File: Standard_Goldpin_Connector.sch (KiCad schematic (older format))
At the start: 1 part, among them P1 Display Connector

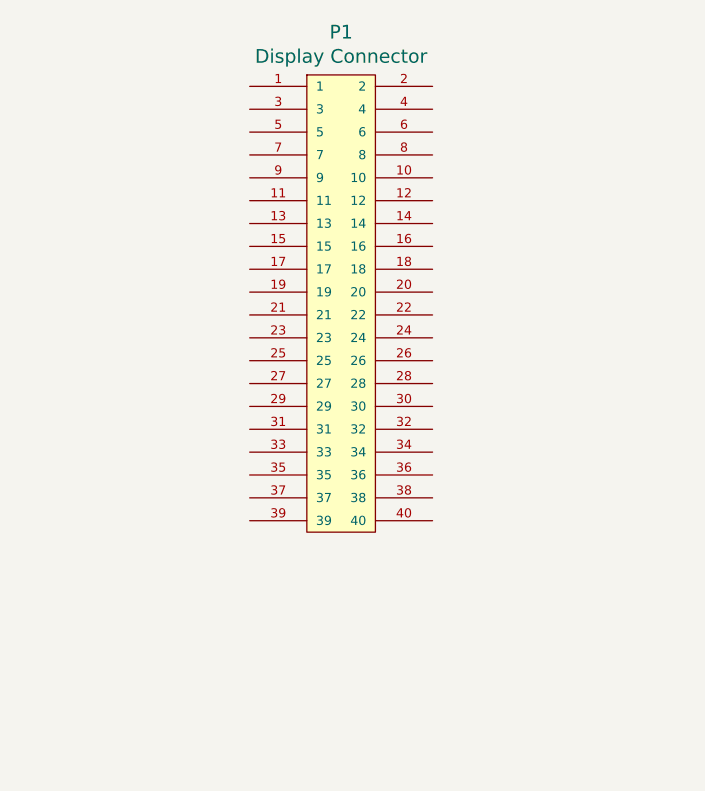
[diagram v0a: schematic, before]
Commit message: Filled hierarchical sheets
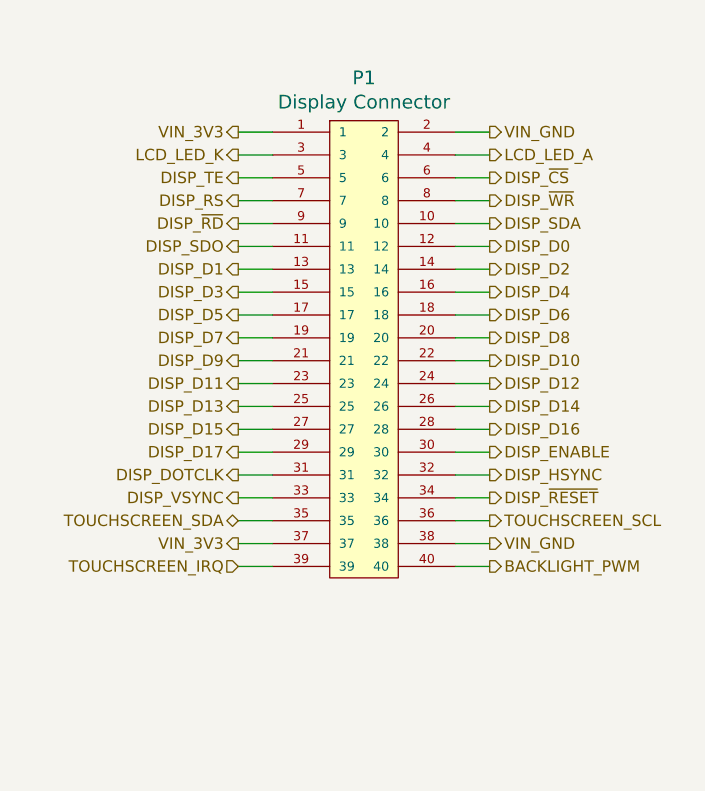
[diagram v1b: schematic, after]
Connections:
- net VIN_3V3: now reaches P1.1
- net VIN_3V3: now also P1.37
- net DISP_SDA: now reaches P1.10
- net DISP_SDO: now reaches P1.11
- net DISP_D0: now reaches P1.12
- net DISP_D1: now reaches P1.13
- net DISP_D2: now reaches P1.14
- net DISP_D3: now reaches P1.15
- net DISP_D4: now reaches P1.16
- net DISP_D5: now reaches P1.17
- net DISP_D6: now reaches P1.18
- net DISP_D7: now reaches P1.19
- net VIN_GND: now reaches P1.2
- net VIN_GND: now also P1.38
- net DISP_D8: now reaches P1.20
- net DISP_D9: now reaches P1.21
- net DISP_D10: now reaches P1.22
- net DISP_D11: now reaches P1.23
- net DISP_D12: now reaches P1.24
- net DISP_D13: now reaches P1.25
- net DISP_D14: now reaches P1.26
- net DISP_D15: now reaches P1.27
- net DISP_D16: now reaches P1.28
- net DISP_D17: now reaches P1.29
- net LCD_LED_K: now reaches P1.3
- net DISP_ENABLE: now reaches P1.30
- net DISP_DOTCLK: now reaches P1.31
- net DISP_HSYNC: now reaches P1.32
- net DISP_VSYNC: now reaches P1.33
- net DISP_~RESET~: now reaches P1.34
- net TOUCHSCREEN_SDA: now reaches P1.35
- net TOUCHSCREEN_SCL: now reaches P1.36
- net TOUCHSCREEN_IRQ: now reaches P1.39
- net LCD_LED_A: now reaches P1.4
- net BACKLIGHT_PWM: now reaches P1.40
- net DISP_TE: now reaches P1.5
- net DISP_~CS~: now reaches P1.6
- net DISP_RS: now reaches P1.7
- net DISP_~WR~: now reaches P1.8
- net DISP_~RD~: now reaches P1.9
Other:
- moved on the sheet: P1
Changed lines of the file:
@@
 $Descr A3 16535 11693
 encoding utf-8
-Sheet 5 5
+Sheet 4 5
 Title "Goldpin Display Connector"
 Date "2020-07-08"
@@
 L Goldpin_2_54mm:GOLDPIN_20_2_2_54MM P1
 U 1 1 5F087B95
-P 8200 5500
-F 0 "P1" H 8200 6687 60  0000 C CNN
-F 1 "Display Connector" H 8200 6581 60  0000 C CNN
-F 2 "Goldpin:Goldpin_20_2_2_54mm_SMT" H 9500 6100 60  0001 C CNN
-F 3 "Goldpins/Components_Documentation/Goldpin_2_54mm.pdf" H 8200 6581 60  0001 C CNN
-	1    8200 5500
+P 8300 5700
+F 0 "P1" H 8300 6887 60  0000 C CNN
+F 1 "Display Connector" H 8300 6781 60  0000 C CNN
+F 2 "Goldpin:Goldpin_20_2_2_54mm_SMT" H 9600 6300 60  0001 C CNN
+F 3 "Goldpins/Components_Documentation/Goldpin_2_54mm.pdf" H 8300 6781 60  0001 C CNN
+	1    8300 5700
 	1    0    0    -1
 $EndComp
+Text HLabel 7750 6650 0    50   Input ~ 0
+TOUCHSCREEN_IRQ
+Text HLabel 7750 6450 0    50   BiDi ~ 0
+TOUCHSCREEN_SDA
+Text HLabel 8850 6450 2    50   Output ~ 0
+TOUCHSCREEN_SCL
+Text HLabel 7750 4750 0    50   Output ~ 0
+VIN_3V3
+Text HLabel 8850 4750 2    50   Output ~ 0
+VIN_GND
+Text HLabel 8850 6650 2    50   Output ~ 0
+BACKLIGHT_PWM
+Text HLabel 7750 4950 0    50   Output ~ 0
+DISP_TE
+Text HLabel 8850 4950 2    50   Output ~ 0
+DISP_~CS~
+Text HLabel 7750 5050 0    50   Output ~ 0
+DISP_RS
+Text HLabel 8850 5050 2    50   Output ~ 0
+DISP_~WR~
+Text HLabel 7750 5150 0    50   Output ~ 0
+DISP_~RD~
+Text HLabel 8850 5150 2    50   Output ~ 0
+DISP_SDA
+Text HLabel 7750 5250 0    50   Output ~ 0
+DISP_SDO
+Text HLabel 8850 5250 2    50   Output ~ 0
+DISP_D0
+Text HLabel 7750 5350 0    50   Output ~ 0
+DISP_D1
+Text HLabel 8850 5350 2    50   Output ~ 0
+DISP_D2
+Text HLabel 7750 5450 0    50   Output ~ 0
+DISP_D3
+Text HLabel 8850 5450 2    50   Output ~ 0
+DISP_D4
+Text HLabel 7750 5550 0    50   Output ~ 0
+DISP_D5
+Text HLabel 8850 5550 2    50   Output ~ 0
+DISP_D6
+Text HLabel 7750 5650 0    50   Output ~ 0
+DISP_D7
+Text HLabel 8850 5650 2    50   Output ~ 0
+DISP_D8
+Text HLabel 7750 5750 0    50   Output ~ 0
+DISP_D9
+Text HLabel 8850 5750 2    50   Output ~ 0
+DISP_D10
+Text HLabel 7750 5850 0    50   Output ~ 0
+DISP_D11
+Text HLabel 8850 5850 2    50   Output ~ 0
+DISP_D12
+Text HLabel 7750 5950 0    50   Output ~ 0
+DISP_D13
+Text HLabel 8850 5950 2    50   Output ~ 0
+DISP_D14
+Text HLabel 7750 6050 0    50   Output ~ 0
+DISP_D15
+Text HLabel 8850 6050 2    50   Output ~ 0
+DISP_D16
+Text HLabel 7750 6150 0    50   Output ~ 0
+DISP_D17
+Text HLabel 8850 6150 2    50   Output ~ 0
+DISP_ENABLE
+Text HLabel 7750 6250 0    50   Output ~ 0
+DISP_DOTCLK
+Text HLabel 8850 6250 2    50   Output ~ 0
+DISP_HSYNC
+Text HLabel 7750 6350 0    50   Output ~ 0
+DISP_VSYNC
+Text HLabel 8850 6350 2    50   Output ~ 0
+DISP_~RESET~
+Text HLabel 7750 4850 0    50   Output ~ 0
+LCD_LED_K
+Text HLabel 8850 4850 2    50   Output ~ 0
+LCD_LED_A
+Text HLabel 8850 6550 2    50   Output ~ 0
+VIN_GND
+Text HLabel 7750 6550 0    50   Output ~ 0
+VIN_3V3
+Wire Wire Line
+	8850 4750 8700 4750
+Wire Wire Line
+	8850 4850 8700 4850
+Wire Wire Line
+	8850 4950 8700 4950
+Wire Wire Line
+	8850 5050 8700 5050
+Wire Wire Line
+	8850 5150 8700 5150
+Wire Wire Line
+	8700 5250 8850 5250
+Wire Wire Line
+	8850 5350 8700 5350
+Wire Wire Line
+	8850 5450 8700 5450
+Wire Wire Line
+	8850 5550 8700 5550
+Wire Wire Line
+	8850 5650 8700 5650
+Wire Wire Line
+	8850 5750 8700 5750
+Wire Wire Line
+	8850 5850 8700 5850
+Wire Wire Line
+	8700 5950 8850 5950
+Wire Wire Line
+	8850 6050 8700 6050
+Wire Wire Line
+	8850 6150 8700 6150
+Wire Wire Line
+	8850 6250 8700 6250
+Wire Wire Line
+	8850 6350 8700 6350
+Wire Wire Line
+	8850 6450 8700 6450
+Wire Wire Line
+	8850 6550 8700 6550
+Wire Wire Line
+	8850 6650 8700 6650
+Wire Wire Line
+	7900 4750 7750 4750
+Wire Wire Line
+	7900 4850 7750 4850
+Wire Wire Line
+	7900 4950 7750 4950
+Wire Wire Line
+	7900 5050 7750 5050
+Wire Wire Line
+	7900 5150 7750 5150
+Wire Wire Line
+	7750 5250 7900 5250
+Wire Wire Line
+	7900 5350 7750 5350
+Wire Wire Line
+	7900 5450 7750 5450
+Wire Wire Line
+	7900 5550 7750 5550
+Wire Wire Line
+	7900 5650 7750 5650
+Wire Wire Line
+	7900 5750 7750 5750
+Wire Wire Line
+	7900 5850 7750 5850
+Wire Wire Line
+	7750 5950 7900 5950
+Wire Wire Line
+	7900 6050 7750 6050
+Wire Wire Line
+	7900 6150 7750 6150
+Wire Wire Line
+	7900 6250 7750 6250
+Wire Wire Line
+	7900 6350 7750 6350
+Wire Wire Line
+	7900 6450 7750 6450
+Wire Wire Line
+	7900 6550 7750 6550
+Wire Wire Line
+	7900 6650 7750 6650
 $EndSCHEMATC

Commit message: Schematic ready, need check
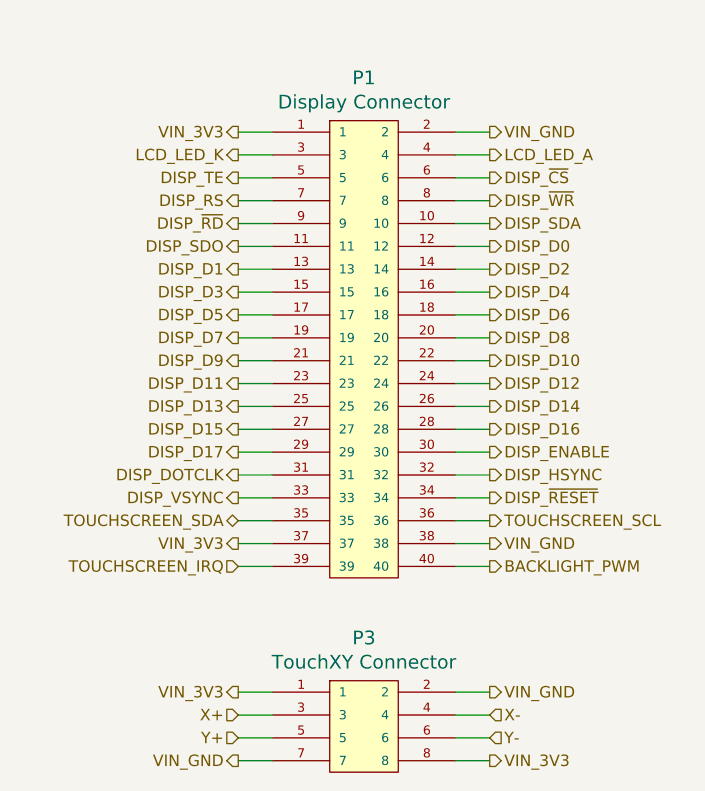
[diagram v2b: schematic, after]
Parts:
- added P3: TouchXY Connector, Goldpin:Goldpin_4_2_2_54mm_SMT, symbol Goldpin_2_54mm:GOLDPIN_4_2_2_54MM
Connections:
- net VIN_3V3: now also P3.1, P3.8
- net VIN_GND: now also P3.2, P3.7
- new net X+: P3.3
- new net X-: P3.4
- new net Y+: P3.5
- new net Y-: P3.6
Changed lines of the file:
@@
 Wire Wire Line
 	7900 6650 7750 6650
+$Comp
+L Goldpin_2_54mm:GOLDPIN_4_2_2_54MM P3
+U 1 1 5F09FA54
+P 8300 7350
+F 0 "P3" H 8300 7737 60  0000 C CNN
+F 1 "TouchXY Connector" H 8300 7631 60  0000 C CNN
+F 2 "Goldpin:Goldpin_4_2_2_54mm_SMT" H 9600 7950 60  0001 C CNN
+F 3 "Goldpins/Components_Documentation/Goldpin_2_54mm.pdf" H 8300 7631 60  0001 C CNN
+	1    8300 7350
+	1    0    0    -1
+$EndComp
+Text HLabel 7750 7200 0    50   Output ~ 0
+VIN_3V3
+Wire Wire Line
+	7900 7200 7750 7200
+Text HLabel 8850 7200 2    50   Output ~ 0
+VIN_GND
+Wire Wire Line
+	8850 7200 8700 7200
+Text HLabel 8850 7300 2    50   Input ~ 0
+X-
+Wire Wire Line
+	8850 7300 8700 7300
+Text HLabel 7750 7300 0    50   Input ~ 0
+X+
+Wire Wire Line
+	7900 7300 7750 7300
+Text HLabel 8850 7400 2    50   Input ~ 0
+Y-
+Wire Wire Line
+	8850 7400 8700 7400
+Text HLabel 7750 7400 0    50   Input ~ 0
+Y+
+Wire Wire Line
+	7900 7400 7750 7400
+Wire Wire Line
+	8850 7500 8700 7500
+Text HLabel 7750 7500 0    50   Output ~ 0
+VIN_GND
+Wire Wire Line
+	7750 7500 7900 7500
+Text HLabel 8850 7500 2    50   Output ~ 0
+VIN_3V3
 $EndSCHEMATC

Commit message: Tracking in progress
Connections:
- net VIN_3V3: now also P3.7; no longer P3.8
- net VIN_GND: now also P3.8; no longer P3.7
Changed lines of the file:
@@
 Wire Wire Line
 	8850 7500 8700 7500
-Text HLabel 7750 7500 0    50   Output ~ 0
+Text HLabel 8850 7500 2    50   Output ~ 0
 VIN_GND
 Wire Wire Line
 	7750 7500 7900 7500
-Text HLabel 8850 7500 2    50   Output ~ 0
+Text HLabel 7750 7500 0    50   Output ~ 0
 VIN_3V3
 $EndSCHEMATC

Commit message: Generated gerbers
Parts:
- removed P3: TouchXY Connector, Goldpin:Goldpin_4_2_2_54mm_SMT, symbol Goldpin_2_54mm:GOLDPIN_4_2_2_54MM
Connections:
- net VIN_3V3: no longer P1.37
- new net TOUCHSCREEN_RESET: P1.37
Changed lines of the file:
@@
 VIN_GND
 Text HLabel 7750 6550 0    50   Output ~ 0
-VIN_3V3
+TOUCHSCREEN_RESET
 Wire Wire Line
 	8850 4750 8700 4750
@@
 Wire Wire Line
 	7900 6650 7750 6650
-$Comp
-L Goldpin_2_54mm:GOLDPIN_4_2_2_54MM P3
-U 1 1 5F09FA54
-P 8300 7350
-F 0 "P3" H 8300 7737 60  0000 C CNN
-F 1 "TouchXY Connector" H 8300 7631 60  0000 C CNN
-F 2 "Goldpin:Goldpin_4_2_2_54mm_SMT" H 9600 7950 60  0001 C CNN
-F 3 "Goldpins/Components_Documentation/Goldpin_2_54mm.pdf" H 8300 7631 60  0001 C CNN
-	1    8300 7350
-	1    0    0    -1
-$EndComp
-Text HLabel 7750 7200 0    50   Output ~ 0
-VIN_3V3
-Wire Wire Line
-	7900 7200 7750 7200
-Text HLabel 8850 7200 2    50   Output ~ 0
-VIN_GND
-Wire Wire Line
-	8850 7200 8700 7200
-Text HLabel 8850 7300 2    50   Input ~ 0
-X-
-Wire Wire Line
-	8850 7300 8700 7300
-Text HLabel 7750 7300 0    50   Input ~ 0
-X+
-Wire Wire Line
-	7900 7300 7750 7300
-Text HLabel 8850 7400 2    50   Input ~ 0
-Y-
-Wire Wire Line
-	8850 7400 8700 7400
-Text HLabel 7750 7400 0    50   Input ~ 0
-Y+
-Wire Wire Line
-	7900 7400 7750 7400
-Wire Wire Line
-	8850 7500 8700 7500
-Text HLabel 8850 7500 2    50   Output ~ 0
-VIN_GND
-Wire Wire Line
-	7750 7500 7900 7500
-Text HLabel 7750 7500 0    50   Output ~ 0
-VIN_3V3
 $EndSCHEMATC
